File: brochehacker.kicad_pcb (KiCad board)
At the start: 2 copper layers, 5 parts, among them IC1 ATTINY85-P, P1 CONN_01X02, U1 MAX7219

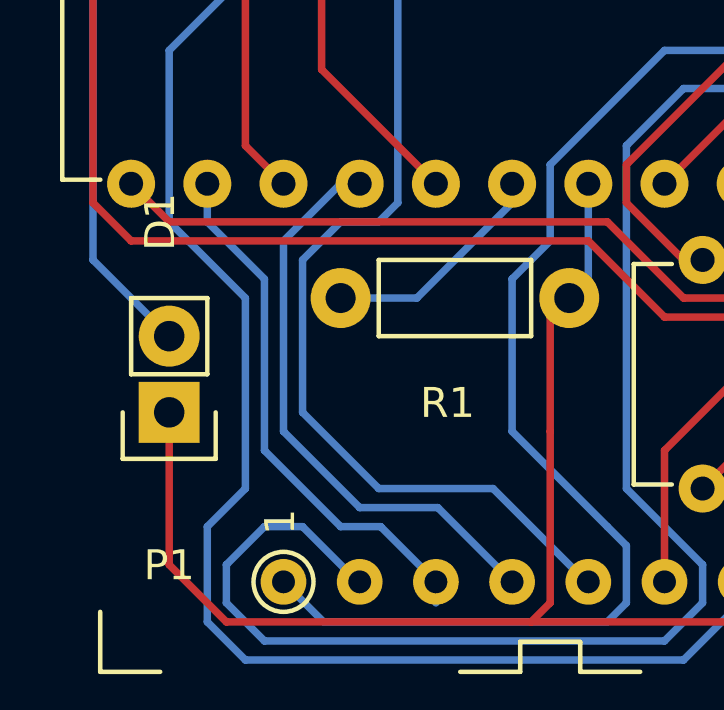
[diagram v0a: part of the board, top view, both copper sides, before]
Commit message: conserta traço perto de pad
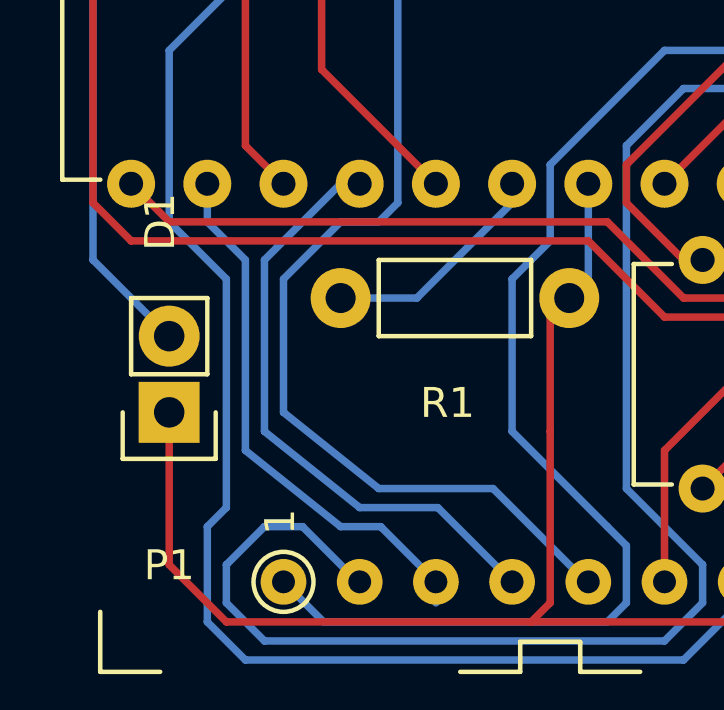
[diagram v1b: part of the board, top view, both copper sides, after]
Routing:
- net /DIG7: track 29.7 -> 30.4 mm
- net /SEGB: track 19.4 -> 20.1 mm
- net /DIG5: track 45.5 -> 45.0 mm
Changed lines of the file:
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@@
     (links 26)
     (no_connects 0)
-    (area 0 0 0 0)
+    (area 166.341667 85.324999 204.315 117.875001)
     (thickness 1.6)
     (drawings 0)
-    (tracks 165)
+    (tracks 164)
     (zones 0)
     (modules 5)
@@
   (segment (start 178.5 111.76) (end 180.34 113.6) (width 0.25) (layer B.Cu) (net 3))
   (segment (start 177.165 111.76) (end 178.5 111.76) (width 0.25) (layer B.Cu) (net 3))
-  (segment (start 174.625 109.22) (end 177.165 111.76) (width 0.25) (layer B.Cu) (net 3))
-  (segment (start 174.625 103.505) (end 174.625 109.22) (width 0.25) (layer B.Cu) (net 3))
-  (segment (start 172.72 101.6) (end 174.625 103.505) (width 0.25) (layer B.Cu) (net 3))
+  (segment (start 173.99 109.22) (end 177.165 111.76) (width 0.25) (layer B.Cu) (net 3))
+  (segment (start 173.99 102.87) (end 173.99 109.22) (width 0.25) (layer B.Cu) (net 3))
+  (segment (start 172.72 101.6) (end 173.99 102.87) (width 0.25) (layer B.Cu) (net 3))
   (segment (start 180.34 113.6) (end 180.275 113.6) (width 0.25) (layer B.Cu) (net 3))
   (segment (start 180.34 113.6) (end 180.34 114.3) (width 0.25) (layer B.Cu) (net 3))
-  (segment (start 177.165 100.33) (end 175.26 102.235) (width 0.25) (layer B.Cu) (net 4))
+  (segment (start 177.165 100.33) (end 174.625 102.87) (width 0.25) (layer B.Cu) (net 4))
   (segment (start 180.405 111.125) (end 182.88 113.6) (width 0.25) (layer B.Cu) (net 4))
   (segment (start 177.8 111.125) (end 180.405 111.125) (width 0.25) (layer B.Cu) (net 4))
-  (segment (start 175.26 108.585) (end 177.8 111.125) (width 0.25) (layer B.Cu) (net 4))
-  (segment (start 175.26 102.235) (end 175.26 108.585) (width 0.25) (layer B.Cu) (net 4))
+  (segment (start 174.625 108.585) (end 177.8 111.125) (width 0.25) (layer B.Cu) (net 4))
+  (segment (start 174.625 102.87) (end 174.625 108.585) (width 0.25) (layer B.Cu) (net 4))
   (segment (start 177.8 100.33) (end 177.165 100.33) (width 0.25) (layer B.Cu) (net 4))
+  (segment (start 175.26 103.505) (end 177.165 101.6) (width 0.25) (layer B.Cu) (net 5))
   (segment (start 179.07 93.98) (end 180.34 92.71) (width 0.25) (layer B.Cu) (net 5))
+  (segment (start 177.165 101.6) (end 178.435 101.6) (width 0.25) (layer B.Cu) (net 5))
+  (segment (start 178.435 101.6) (end 179.07 100.965) (width 0.25) (layer B.Cu) (net 5))
   (segment (start 179.07 100.965) (end 179.07 93.98) (width 0.25) (layer B.Cu) (net 5))
-  (segment (start 178.435 101.6) (end 179.07 100.965) (width 0.25) (layer B.Cu) (net 5))
-  (segment (start 177.165 101.6) (end 178.435 101.6) (width 0.25) (layer B.Cu) (net 5))
-  (segment (start 175.895 102.87) (end 177.165 101.6) (width 0.25) (layer B.Cu) (net 5))
   (segment (start 185.42 113.6) (end 185.355 113.6) (width 0.25) (layer B.Cu) (net 5))
   (segment (start 185.355 113.6) (end 182.245 110.49) (width 0.25) (layer B.Cu) (net 5))
-  (segment (start 175.895 107.95) (end 175.895 102.87) (width 0.25) (layer B.Cu) (net 5))
-  (segment (start 178.435 110.49) (end 175.895 107.95) (width 0.25) (layer B.Cu) (net 5))
+  (segment (start 175.26 107.95) (end 175.26 103.505) (width 0.25) (layer B.Cu) (net 5))
+  (segment (start 178.435 110.49) (end 175.26 107.95) (width 0.25) (layer B.Cu) (net 5))
   (segment (start 182.245 110.49) (end 178.435 110.49) (width 0.25) (layer B.Cu) (net 5))
-  (segment (start 175.895 102.87) (end 175.895 102.87) (width 0.25) (layer B.Cu) (net 5))
   (segment (start 187.96 113.6) (end 187.96 109.22) (width 0.25) (layer F.Cu) (net 6))
   (segment (start 195.58 103.505) (end 195.58 100.33) (width 0.25) (layer F.Cu) (net 6))
@@
   (segment (start 172.72 114.935) (end 173.99 116.205) (width 0.25) (layer B.Cu) (net 7))
   (segment (start 172.72 111.76) (end 172.72 114.935) (width 0.25) (layer B.Cu) (net 7))
-  (segment (start 173.99 110.49) (end 172.72 111.76) (width 0.25) (layer B.Cu) (net 7))
-  (segment (start 173.99 104.14) (end 173.99 110.49) (width 0.25) (layer B.Cu) (net 7))
-  (segment (start 171.45 101.6) (end 173.99 104.14) (width 0.25) (layer B.Cu) (net 7))
+  (segment (start 173.355 111.125) (end 172.72 111.76) (width 0.25) (layer B.Cu) (net 7))
+  (segment (start 173.355 103.505) (end 173.355 111.125) (width 0.25) (layer B.Cu) (net 7))
+  (segment (start 171.45 101.6) (end 173.355 103.505) (width 0.25) (layer B.Cu) (net 7))
   (segment (start 171.45 95.885) (end 171.45 101.6) (width 0.25) (layer B.Cu) (net 7))
   (segment (start 174.625 92.71) (end 171.45 95.885) (width 0.25) (layer B.Cu) (net 7))

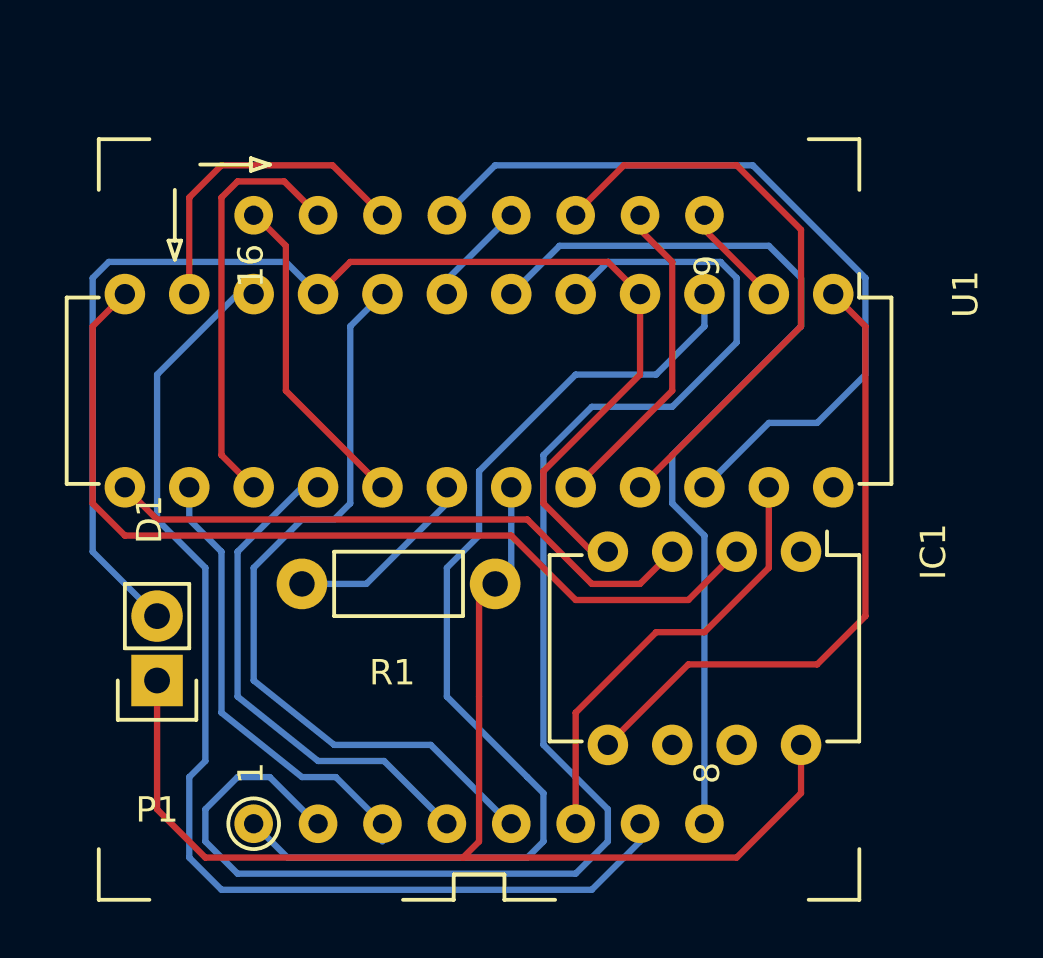
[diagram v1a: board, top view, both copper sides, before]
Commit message: correção da orientação do display
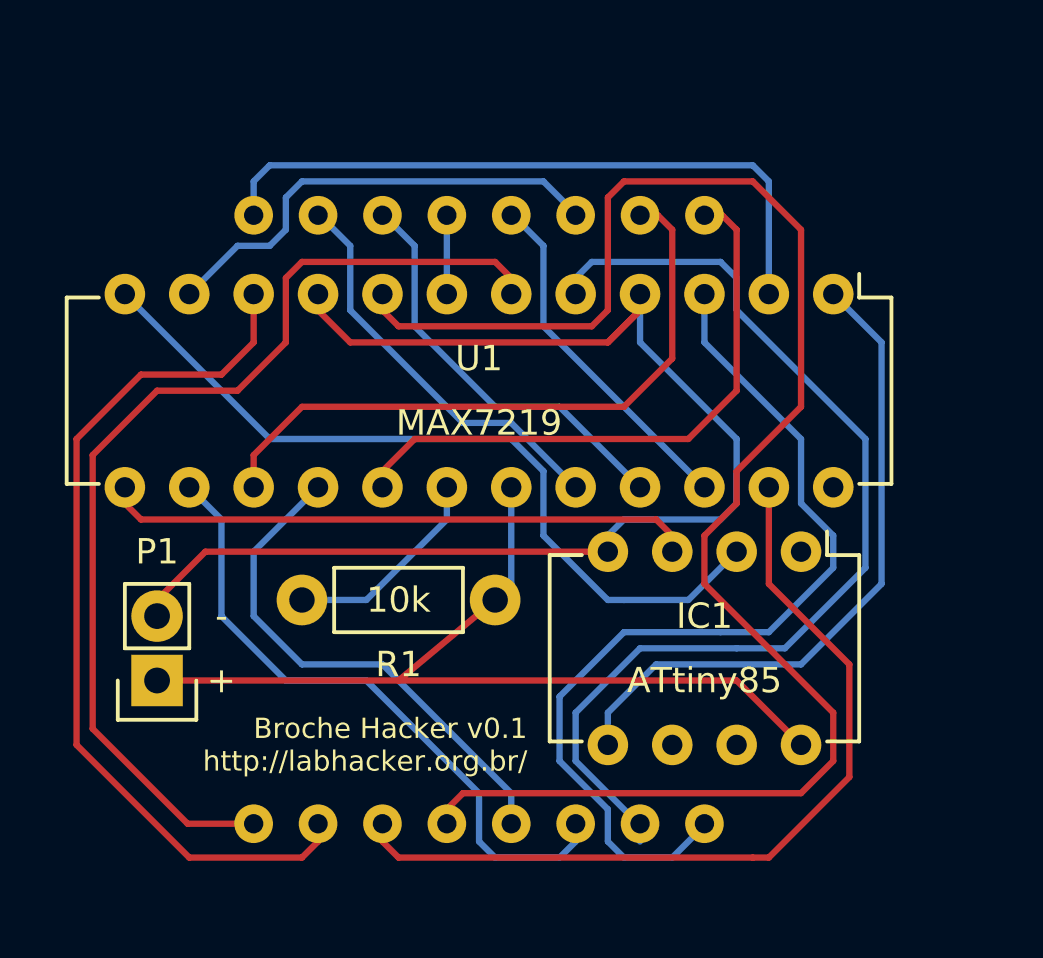
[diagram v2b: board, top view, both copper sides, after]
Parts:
- D1: moved to B.Cu
- moved R1 0.64 mm to (184.8, 104.8)
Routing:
- net /DIG7: track 30.4 -> 64.4 mm
- net /DIG0: track 4.16 -> 26.8 mm
- net /DIG6: track 59.4 -> 41.0 mm
- net /SEGDP: track 31.8 -> 13.9 mm
- net /SEGD: track 18.2 -> 34.1 mm
- net /SEGG: track 12.9 -> 25.0 mm
- net VCC: track 49.6 -> 37.9 mm
- net /DIG5: track 45.0 -> 34.9 mm
- net /SEGF: track 16.6 -> 26.5 mm
- net /SEGA: track 18.2 -> 25.7 mm
- net /SEGE: track 23.6 -> 16.5 mm
- net /DIG1: track 12.8 -> 18.4 mm
- net Net-(IC1-Pad2): track 36.5 -> 31.4 mm
- net /DIG4: track 41.5 -> 37.0 mm
- net /DIG2: track 36.9 -> 40.7 mm
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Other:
- net class Default: clearance 0.2 -> 0.16
- rule trace_clearance: 0.2 -> 0.16
- rule trace_min: 0.2 -> 0.16
- rule via_min_drill: 0.3 -> 0.16
- board text added: "+"
- board text added: "-"
- board text added: "ATtiny85"
- board text added: "Broche Hacker v0.1 http://labhacker.org.br/"
- board text added: "MAX7219"

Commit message: adição de espaço em cobre para soldar um alfinete
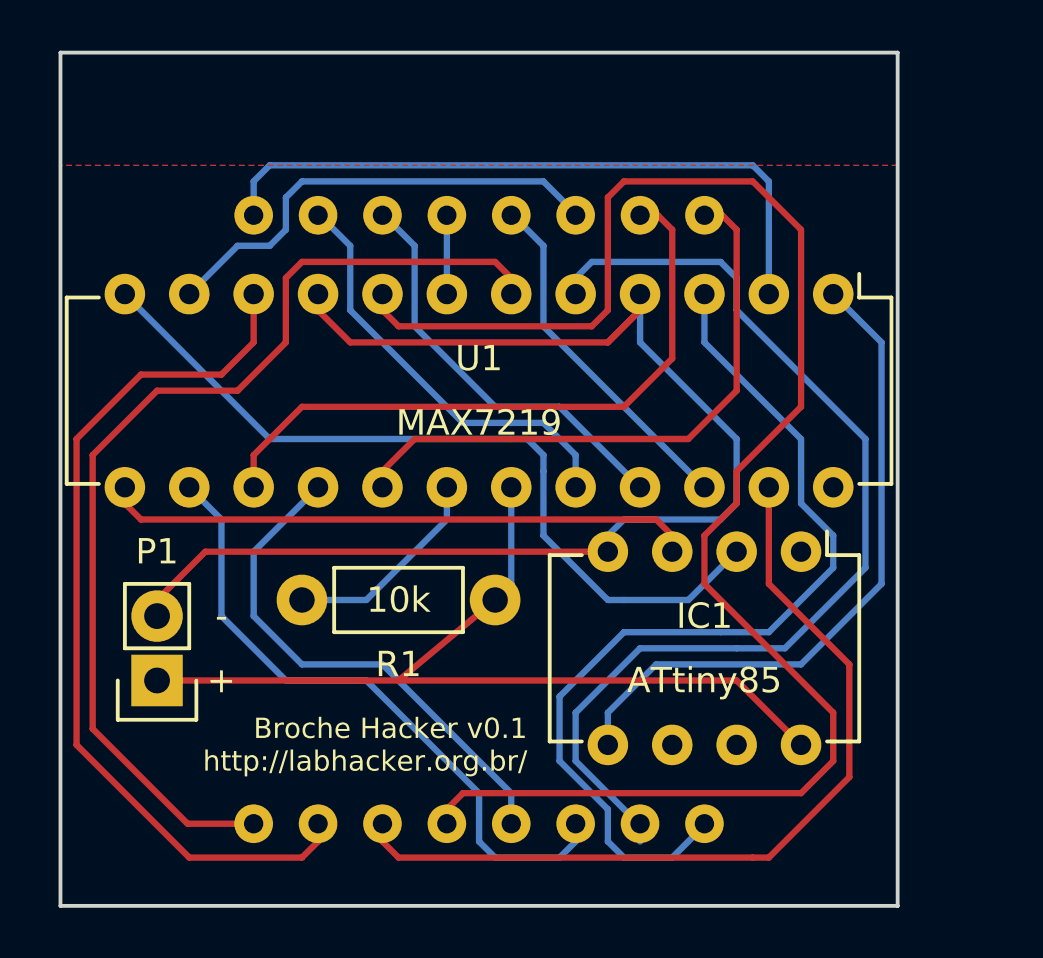
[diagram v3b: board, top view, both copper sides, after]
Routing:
- net /SEGC: track 16.1 -> 16.8 mm
- added copper zone on F.Cu, net (none)
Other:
- board outline added: 33 x 33.7 mm
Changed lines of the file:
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@@
     (links 26)
     (no_connects 0)
-    (area 165.285 85.364999 202.775 117.835001)
+    (area 167.564999 83.109999 200.735001 116.915001)
     (thickness 1.6)
-    (drawings 5)
-    (tracks 201)
+    (drawings 9)
+    (tracks 205)
     (zones 0)
     (modules 5)
@@
   (page A4)
   (layers
-    (0 F.Cu signal hide)
+    (0 F.Cu signal)
     (31 B.Cu signal)
     (36 B.SilkS user)
@@
     )
   )
+  (gr_line (start 167.64 83.185) (end 167.64 116.84) (angle 90) (layer Edge.Cuts) (width 0.15))
+  (gr_line (start 200.66 83.185) (end 167.64 83.185) (angle 90) (layer Edge.Cuts) (width 0.15))
+  (gr_line (start 200.66 116.84) (end 200.66 83.185) (angle 90) (layer Edge.Cuts) (width 0.15))
+  (gr_line (start 167.64 116.84) (end 200.66 116.84) (angle 90) (layer Edge.Cuts) (width 0.15))
   (gr_text ATtiny85 (at 193.04 107.95) (layer F.SilkS)
     (effects (font (size 1 1) (thickness 0.2)))
@@
   (segment (start 198.12 109.22) (end 198.12 111.125) (width 0.25) (layer F.Cu) (net 5))
   (segment (start 182.88 113.03) (end 182.88 113.6) (width 0.25) (layer F.Cu) (net 5))
+  (segment (start 180.34 113.6) (end 180.275 113.6) (width 0.25) (layer B.Cu) (net 6))
   (segment (start 194.945 114.935) (end 195.58 114.935) (width 0.25) (layer F.Cu) (net 6))
   (segment (start 198.755 107.315) (end 195.58 104.14) (width 0.25) (layer F.Cu) (net 6))
@@
   (segment (start 195.58 104.14) (end 195.58 100.33) (width 0.25) (layer F.Cu) (net 6))
   (segment (start 180.34 113.6) (end 180.405 113.6) (width 0.25) (layer F.Cu) (net 6))
-  (segment (start 180.34 113.6) (end 180.275 113.6) (width 0.25) (layer B.Cu) (net 6))
+  (segment (start 177.8 113.6) (end 177.735 113.6) (width 0.25) (layer B.Cu) (net 7))
   (segment (start 177.8 113.6) (end 177.8 114.3) (width 0.25) (layer F.Cu) (net 7))
   (segment (start 177.8 114.3) (end 177.165 114.935) (width 0.25) (layer F.Cu) (net 7))
@@
   (segment (start 172.72 114.935) (end 168.275 110.49) (width 0.25) (layer F.Cu) (net 7))
   (segment (start 177.165 114.935) (end 172.72 114.935) (width 0.25) (layer F.Cu) (net 7))
-  (segment (start 177.8 113.6) (end 177.735 113.6) (width 0.25) (layer B.Cu) (net 7))
   (segment (start 177.165 91.44) (end 184.785 91.44) (width 0.25) (layer F.Cu) (net 8))
   (segment (start 176.53 92.075) (end 177.165 91.44) (width 0.25) (layer F.Cu) (net 8))
@@
   (segment (start 174.625 96.52) (end 176.53 94.615) (width 0.25) (layer F.Cu) (net 8))
   (segment (start 185.42 92.075) (end 185.42 92.71) (width 0.25) (layer F.Cu) (net 8))
+  (segment (start 175.325 89.6) (end 175.26 89.6) (width 0.25) (layer F.Cu) (net 9))
+  (segment (start 175.26 89.535) (end 175.26 89.6) (width 0.25) (layer F.Cu) (net 9))
   (segment (start 175.26 89.6) (end 175.26 88.265) (width 0.25) (layer B.Cu) (net 9))
   (segment (start 195.58 88.265) (end 195.58 92.71) (width 0.25) (layer B.Cu) (net 9))
@@
   (segment (start 175.895 87.63) (end 194.945 87.63) (width 0.25) (layer B.Cu) (net 9))
   (segment (start 175.26 88.265) (end 175.895 87.63) (width 0.25) (layer B.Cu) (net 9))
-  (segment (start 175.325 89.6) (end 175.26 89.6) (width 0.25) (layer F.Cu) (net 9))
-  (segment (start 175.26 89.535) (end 175.26 89.6) (width 0.25) (layer F.Cu) (net 9))
+  (segment (start 185.42 97.79) (end 186.69 97.79) (width 0.25) (layer B.Cu) (net 10))
+  (segment (start 187.96 99.06) (end 187.96 100.33) (width 0.25) (layer B.Cu) (net 10))
+  (segment (start 186.69 97.79) (end 187.96 99.06) (width 0.25) (layer B.Cu) (net 10))
   (segment (start 177.8 89.6) (end 177.865 89.6) (width 0.25) (layer B.Cu) (net 10))
   (segment (start 177.865 89.6) (end 179.07 90.805) (width 0.25) (layer B.Cu) (net 10))
@@
   (segment (start 179.07 93.345) (end 183.515 97.79) (width 0.25) (layer B.Cu) (net 10))
   (segment (start 183.515 97.79) (end 185.42 97.79) (width 0.25) (layer B.Cu) (net 10))
-  (segment (start 185.42 97.79) (end 187.96 100.33) (width 0.25) (layer B.Cu) (net 10))
   (segment (start 180.34 89.6) (end 180.405 89.6) (width 0.25) (layer B.Cu) (net 11))
   (segment (start 180.405 89.6) (end 181.61 90.805) (width 0.25) (layer B.Cu) (net 11))
@@
   (segment (start 180.34 100.33) (end 180.34 100.965) (width 0.25) (layer F.Cu) (net 16))
   (segment (start 193.04 89.6) (end 193.04 90.17) (width 0.25) (layer F.Cu) (net 16))
+  (segment (start 185.42 98.425) (end 186.055 98.425) (width 0.25) (layer B.Cu) (net 18))
+  (segment (start 186.69 99.06) (end 186.69 99.695) (width 0.25) (layer B.Cu) (net 18))
+  (segment (start 186.055 98.425) (end 186.69 99.06) (width 0.25) (layer B.Cu) (net 18))
   (segment (start 189.865 104.775) (end 189.23 104.775) (width 0.25) (layer B.Cu) (net 18))
   (segment (start 175.895 98.425) (end 170.18 92.71) (width 0.25) (layer B.Cu) (net 18))
   (segment (start 185.42 98.425) (end 175.895 98.425) (width 0.25) (layer B.Cu) (net 18))
-  (segment (start 186.69 99.695) (end 185.42 98.425) (width 0.25) (layer B.Cu) (net 18))
   (segment (start 186.69 102.235) (end 186.69 99.695) (width 0.25) (layer B.Cu) (net 18))
   (segment (start 189.23 104.775) (end 186.69 102.235) (width 0.25) (layer B.Cu) (net 18))
@@
   (segment (start 179.705 104.775) (end 182.88 101.6) (width 0.25) (layer B.Cu) (net 25))
   (segment (start 182.88 100.33) (end 182.88 100.965) (width 0.25) (layer B.Cu) (net 25))
+  (zone (net 0) (net_name "") (layer F.Cu) (hatch edge 0.508)
+    (connect_pads (clearance 0.4))
+    (min_thickness 0.25)
+    (fill yes (arc_segments 16) (thermal_gap 0.508) (thermal_bridge_width 0.508))
+    (polygon
+      (pts
+        (xy 200.66 87.63) (xy 167.64 87.63) (xy 167.64 83.185) (xy 200.66 83.185) (xy 200.66 87.63)
+      )
+    )
+  )
+  (zone (net 0) (net_name "") (layer F.Mask) (hatch edge 0.508)
+    (connect_pads (clearance 0.4))
+    (min_thickness 0.25)
+    (fill yes (arc_segments 16) (thermal_gap 0.508) (thermal_bridge_width 0.508))
+    (polygon
+      (pts
+        (xy 199.39 86.995) (xy 168.91 86.995) (xy 168.91 83.82) (xy 199.39 83.82) (xy 199.39 86.995)
+      )
+    )
+  )
 )
